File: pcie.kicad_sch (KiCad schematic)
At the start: 21 parts, among them U15 XC7K160T-FFG676

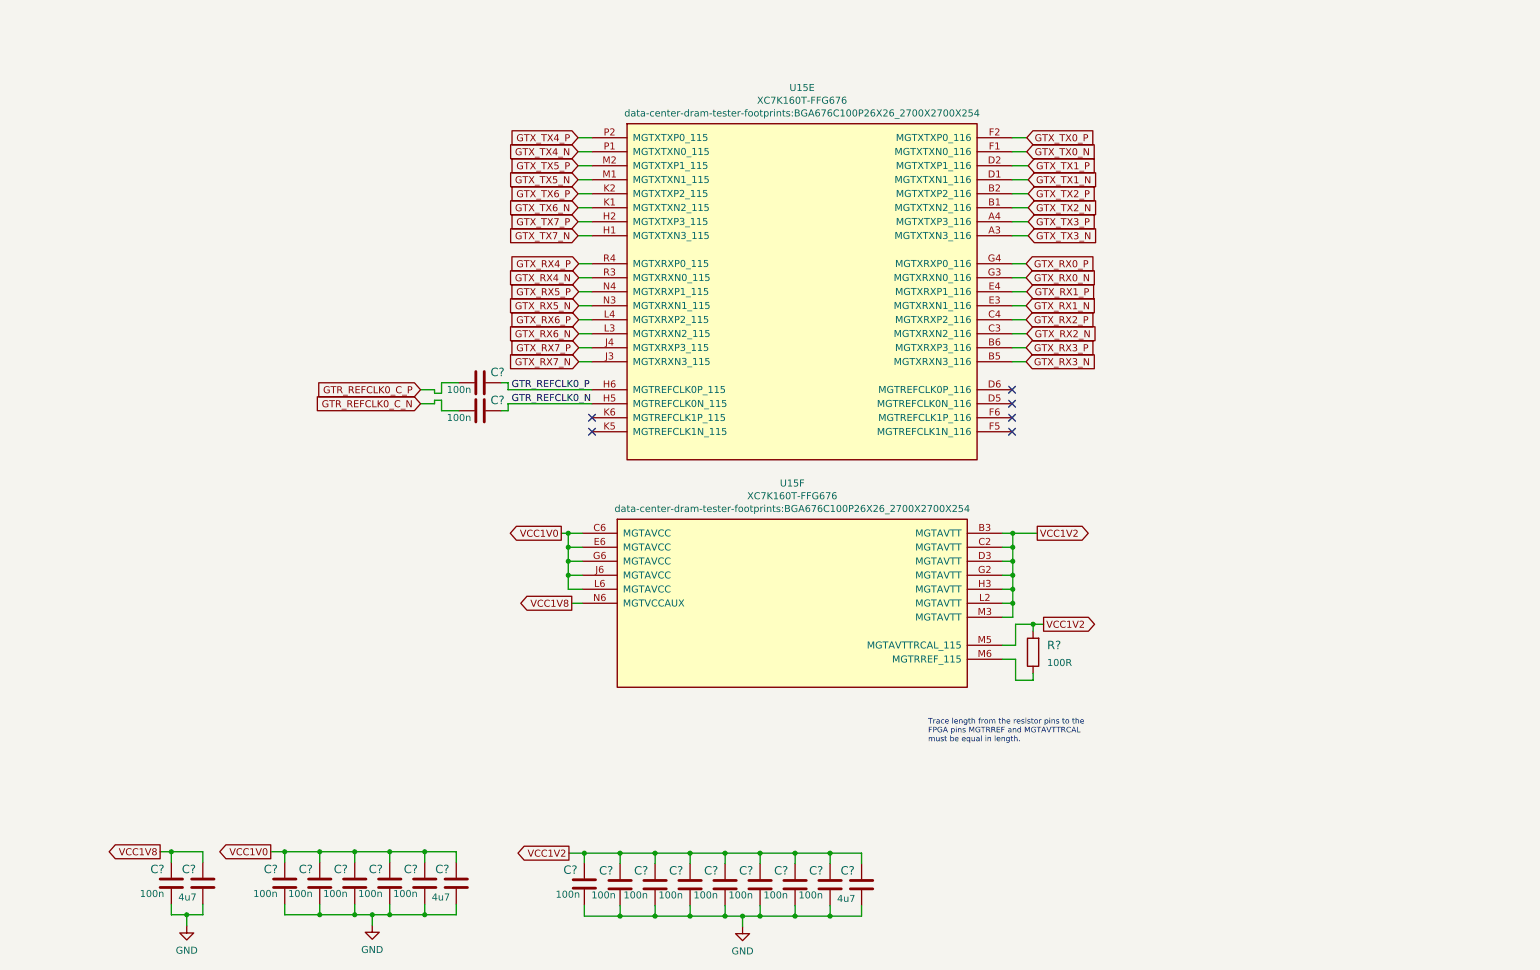
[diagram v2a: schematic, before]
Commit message: Connect ETH mux, connect AUX_JTAG to FMC connector, add RC filter for HOT_SWAP_BUTTON signal
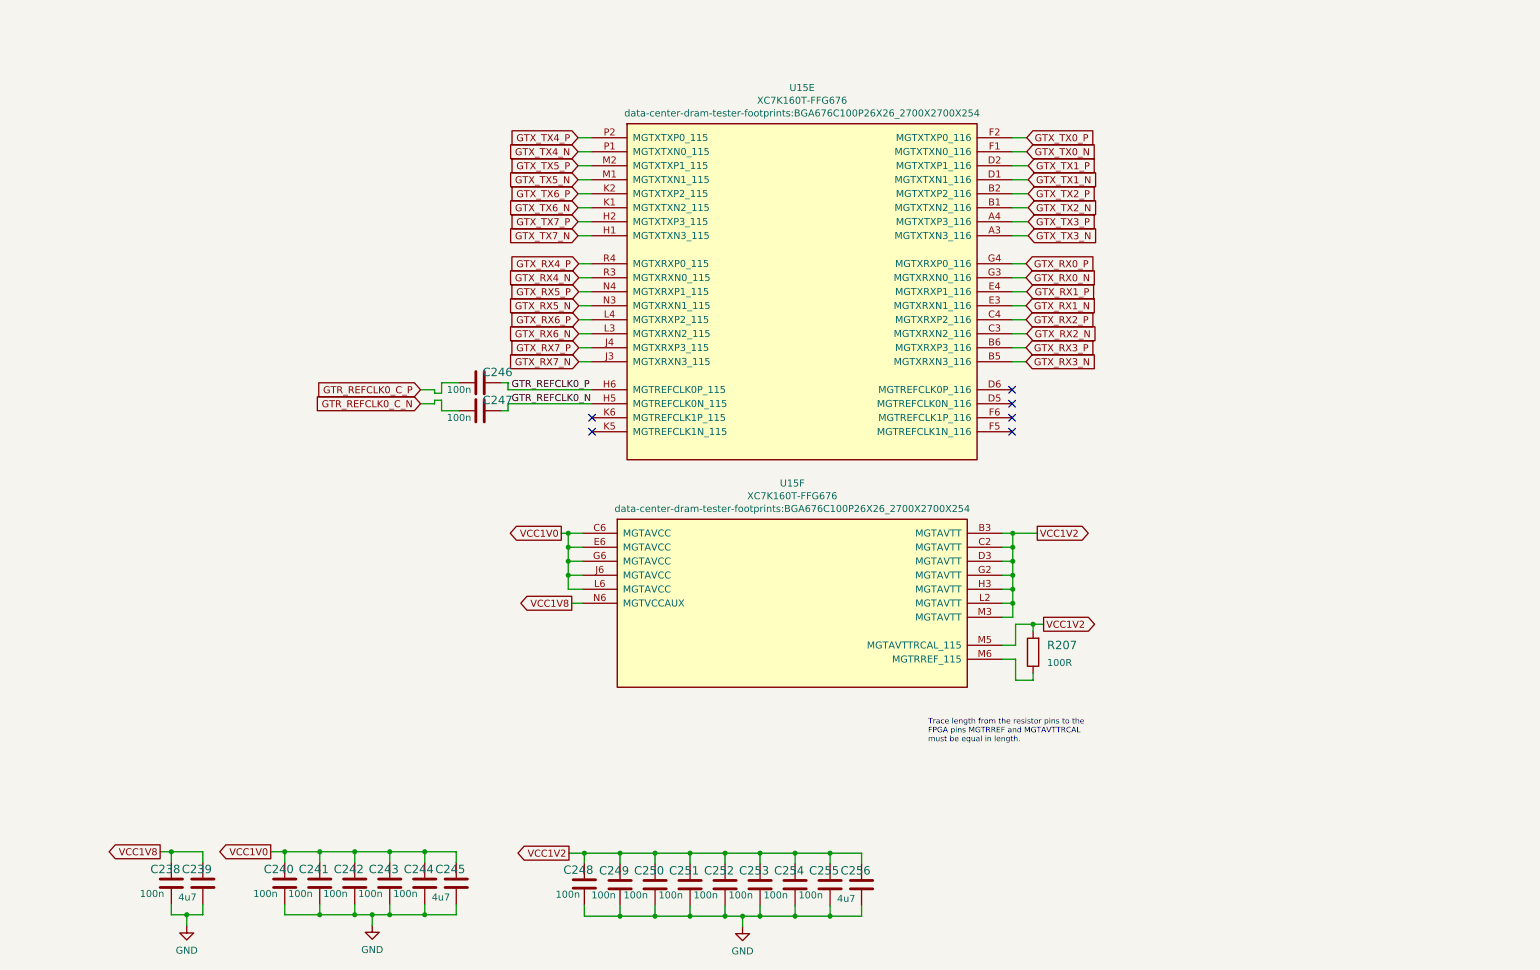
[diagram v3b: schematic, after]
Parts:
- gave numbers to parts that had none: 20
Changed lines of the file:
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@@
   (symbol (lib_id "antmicroCapacitors0402:C_4u7_0402") (at 48.133 178.435 0) (unit 1)
     (in_bom yes) (on_board yes)
-    (property "Reference" "C?" (id 0) (at 44.323 175.895 0)
+    (property "Reference" "C239" (id 0) (at 44.323 175.895 0)
       (effects (font (size 1.524 1.524)) (justify left))
     )
@@
   (symbol (lib_id "antmicroCapacitorsmisc:C_100n_0201") (at 82.042 178.435 0) (unit 1)
     (in_bom yes) (on_board yes)
-    (property "Reference" "C?" (id 0) (at 78.232 175.895 0)
+    (property "Reference" "C243" (id 0) (at 78.232 175.895 0)
       (effects (font (size 1.524 1.524)) (justify left))
     )
@@
   (symbol (lib_id "antmicroCapacitors0402:C_100n_0402") (at 98.425 87.63 90) (unit 1)
     (in_bom yes) (on_board yes)
-    (property "Reference" "C?" (id 0) (at 101.6 85.725 90)
+    (property "Reference" "C246" (id 0) (at 101.6 85.725 90)
       (effects (font (size 1.524 1.524)))
     )
@@
   (symbol (lib_id "antmicroCapacitorsmisc:C_100n_0201") (at 117.348 178.562 0) (unit 1)
     (in_bom yes) (on_board yes)
-    (property "Reference" "C?" (id 0) (at 113.538 176.022 0)
+    (property "Reference" "C248" (id 0) (at 113.538 176.022 0)
       (effects (font (size 1.524 1.524)) (justify left))
     )
@@
   (symbol (lib_id "power:GND") (at 78.867 186.055 0) (unit 1)
     (in_bom yes) (on_board yes) (fields_autoplaced)
-    (property "Reference" "#PWR?" (id 0) (at 78.867 192.405 0)
+    (property "Reference" "#PWR0342" (id 0) (at 78.867 192.405 0)
       (effects (font (size 1.27 1.27)) hide)
     )
@@
   (symbol (lib_id "power:GND") (at 45.212 186.182 0) (unit 1)
     (in_bom yes) (on_board yes) (fields_autoplaced)
-    (property "Reference" "#PWR?" (id 0) (at 45.212 192.532 0)
+    (property "Reference" "#PWR0343" (id 0) (at 45.212 192.532 0)
       (effects (font (size 1.27 1.27)) hide)
     )
@@
   (symbol (lib_id "antmicroCapacitorsmisc:C_100n_0201") (at 149.225 178.689 0) (unit 1)
     (in_bom yes) (on_board yes)
-    (property "Reference" "C?" (id 0) (at 145.415 176.149 0)
+    (property "Reference" "C253" (id 0) (at 145.415 176.149 0)
       (effects (font (size 1.524 1.524)) (justify left))
     )
@@
   (symbol (lib_id "antmicroCapacitorsmisc:C_100n_0201") (at 62.992 178.435 0) (unit 1)
     (in_bom yes) (on_board yes)
-    (property "Reference" "C?" (id 0) (at 59.182 175.895 0)
+    (property "Reference" "C240" (id 0) (at 59.182 175.895 0)
       (effects (font (size 1.524 1.524)) (justify left))
     )
@@
   (symbol (lib_id "antmicroCapacitorsmisc:C_100n_0201") (at 42.418 178.435 0) (unit 1)
     (in_bom yes) (on_board yes)
-    (property "Reference" "C?" (id 0) (at 38.608 175.895 0)
+    (property "Reference" "C238" (id 0) (at 38.608 175.895 0)
       (effects (font (size 1.524 1.524)) (justify left))
     )
@@
   (symbol (lib_id "antmicroCapacitorsmisc:C_100n_0201") (at 130.175 178.689 0) (unit 1)
     (in_bom yes) (on_board yes)
-    (property "Reference" "C?" (id 0) (at 126.365 176.149 0)
+    (property "Reference" "C250" (id 0) (at 126.365 176.149 0)
       (effects (font (size 1.524 1.524)) (justify left))
     )
@@
   (symbol (lib_id "antmicroCapacitorsmisc:C_100n_0201") (at 123.825 178.689 0) (unit 1)
     (in_bom yes) (on_board yes)
-    (property "Reference" "C?" (id 0) (at 120.015 176.149 0)
+    (property "Reference" "C249" (id 0) (at 120.015 176.149 0)
       (effects (font (size 1.524 1.524)) (justify left))
     )
@@
   (symbol (lib_id "antmicroCapacitorsmisc:C_100n_0201") (at 136.525 178.689 0) (unit 1)
     (in_bom yes) (on_board yes)
-    (property "Reference" "C?" (id 0) (at 132.715 176.149 0)
+    (property "Reference" "C251" (id 0) (at 132.715 176.149 0)
       (effects (font (size 1.524 1.524)) (justify left))
     )
@@
   (symbol (lib_id "antmicroCapacitors0402:C_4u7_0402") (at 167.64 178.689 0) (unit 1)
     (in_bom yes) (on_board yes)
-    (property "Reference" "C?" (id 0) (at 163.83 176.149 0)
+    (property "Reference" "C256" (id 0) (at 163.83 176.149 0)
       (effects (font (size 1.524 1.524)) (justify left))
     )
@@
   (symbol (lib_id "antmicroCapacitorsmisc:C_100n_0201") (at 75.692 178.435 0) (unit 1)
     (in_bom yes) (on_board yes)
-    (property "Reference" "C?" (id 0) (at 71.882 175.895 0)
+    (property "Reference" "C242" (id 0) (at 71.882 175.895 0)
       (effects (font (size 1.524 1.524)) (justify left))
     )
@@
   (symbol (lib_id "antmicroCapacitorsmisc:C_100n_0201") (at 69.342 178.435 0) (unit 1)
     (in_bom yes) (on_board yes)
-    (property "Reference" "C?" (id 0) (at 65.532 175.895 0)
+    (property "Reference" "C241" (id 0) (at 65.532 175.895 0)
       (effects (font (size 1.524 1.524)) (justify left))
     )
@@
   (symbol (lib_id "antmicroCapacitorsmisc:C_100n_0201") (at 155.575 178.689 0) (unit 1)
     (in_bom yes) (on_board yes)
-    (property "Reference" "C?" (id 0) (at 151.765 176.149 0)
+    (property "Reference" "C254" (id 0) (at 151.765 176.149 0)
       (effects (font (size 1.524 1.524)) (justify left))
     )
@@
   (symbol (lib_id "antmicroResistors0402:R_100R_0402") (at 198.755 136.525 90) (unit 1)
     (in_bom yes) (on_board yes) (fields_autoplaced)
-    (property "Reference" "R?" (id 0) (at 201.295 135.255 90)
+    (property "Reference" "R207" (id 0) (at 201.295 135.255 90)
       (effects (font (size 1.524 1.524)) (justify right))
     )
@@
   (symbol (lib_id "power:GND") (at 146.05 186.309 0) (unit 1)
     (in_bom yes) (on_board yes) (fields_autoplaced)
-    (property "Reference" "#PWR?" (id 0) (at 146.05 192.659 0)
+    (property "Reference" "#PWR0341" (id 0) (at 146.05 192.659 0)
       (effects (font (size 1.27 1.27)) hide)
     )
@@
   (symbol (lib_id "antmicroCapacitors0402:C_4u7_0402") (at 94.107 178.435 0) (unit 1)
     (in_bom yes) (on_board yes)
-    (property "Reference" "C?" (id 0) (at 90.297 175.895 0)
+    (property "Reference" "C245" (id 0) (at 90.297 175.895 0)
       (effects (font (size 1.524 1.524)) (justify left))
     )
@@
   (symbol (lib_id "antmicroCapacitorsmisc:C_100n_0201") (at 88.392 178.435 0) (unit 1)
     (in_bom yes) (on_board yes)
-    (property "Reference" "C?" (id 0) (at 84.582 175.895 0)
+    (property "Reference" "C244" (id 0) (at 84.582 175.895 0)
       (effects (font (size 1.524 1.524)) (justify left))
     )
@@
   (symbol (lib_id "antmicroCapacitors0402:C_100n_0402") (at 98.425 92.71 90) (unit 1)
     (in_bom yes) (on_board yes)
-    (property "Reference" "C?" (id 0) (at 101.6 90.805 90)
+    (property "Reference" "C247" (id 0) (at 101.6 90.805 90)
       (effects (font (size 1.524 1.524)))
     )
@@
   (symbol (lib_id "antmicroCapacitorsmisc:C_100n_0201") (at 142.875 178.689 0) (unit 1)
     (in_bom yes) (on_board yes)
-    (property "Reference" "C?" (id 0) (at 139.065 176.149 0)
+    (property "Reference" "C252" (id 0) (at 139.065 176.149 0)
       (effects (font (size 1.524 1.524)) (justify left))
     )
@@
   (symbol (lib_id "antmicroCapacitorsmisc:C_100n_0201") (at 161.925 178.689 0) (unit 1)
     (in_bom yes) (on_board yes)
-    (property "Reference" "C?" (id 0) (at 158.115 176.149 0)
+    (property "Reference" "C255" (id 0) (at 158.115 176.149 0)
       (effects (font (size 1.524 1.524)) (justify left))
     )

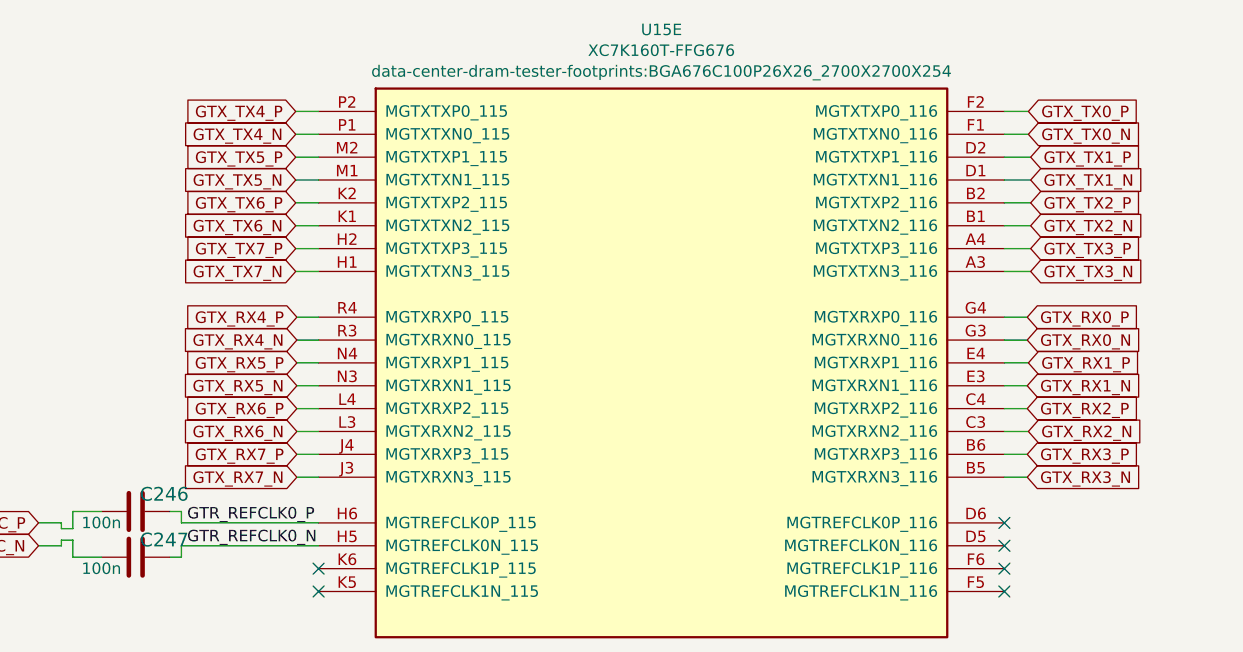
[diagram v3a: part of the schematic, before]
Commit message: Correct PCIe pin assigment, replace MODE2 symbol, export changes to PCB, progess in the new components placement
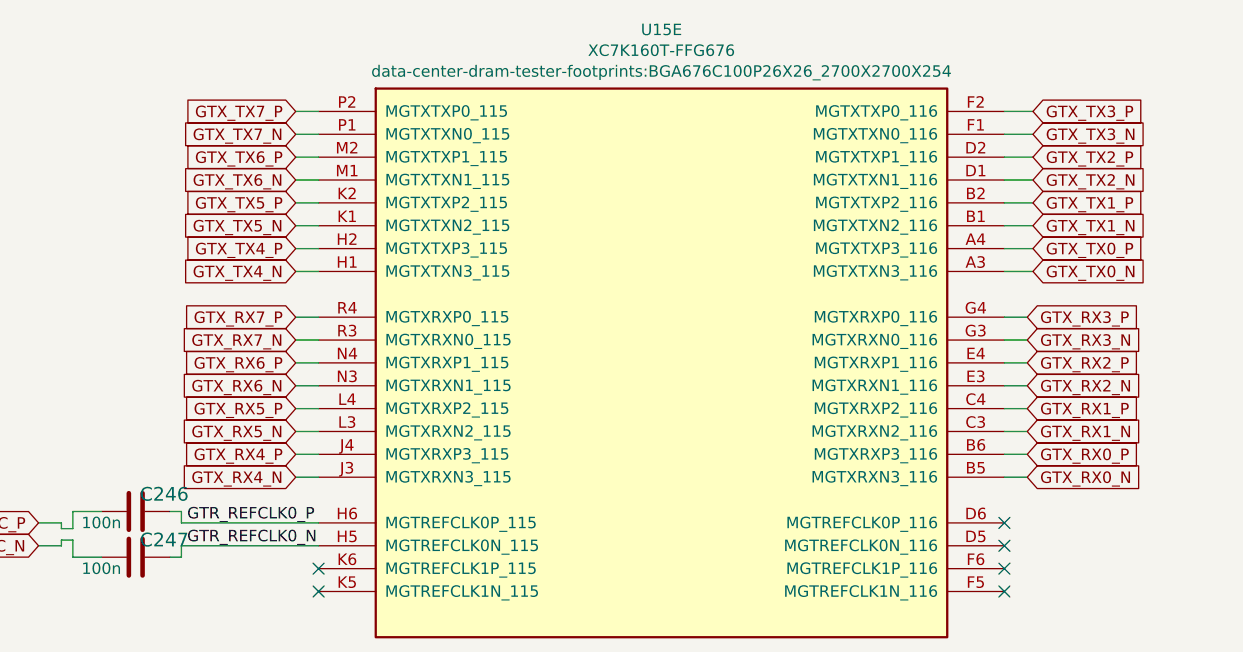
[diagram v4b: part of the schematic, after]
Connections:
- net GTX_RX0_N: now also U15.B5 (MGTXRXN3_116); no longer U15.G3 (MGTXRXN0_116)
- net GTX_RX0_P: now also U15.B6 (MGTXRXP3_116); no longer U15.G4 (MGTXRXP0_116)
- net GTX_RX1_N: now also U15.C3 (MGTXRXN2_116); no longer U15.E3 (MGTXRXN1_116)
- net GTX_RX1_P: now also U15.C4 (MGTXRXP2_116); no longer U15.E4 (MGTXRXP1_116)
- net GTX_RX2_N: now also U15.E3 (MGTXRXN1_116); no longer U15.C3 (MGTXRXN2_116)
- net GTX_RX2_P: now also U15.E4 (MGTXRXP1_116); no longer U15.C4 (MGTXRXP2_116)
- net GTX_RX3_N: now also U15.G3 (MGTXRXN0_116); no longer U15.B5 (MGTXRXN3_116)
- net GTX_RX3_P: now also U15.G4 (MGTXRXP0_116); no longer U15.B6 (MGTXRXP3_116)
- net GTX_RX4_N: now also U15.J3 (MGTXRXN3_115); no longer U15.R3 (MGTXRXN0_115)
- net GTX_RX4_P: now also U15.J4 (MGTXRXP3_115); no longer U15.R4 (MGTXRXP0_115)
- net GTX_RX5_N: now also U15.L3 (MGTXRXN2_115); no longer U15.N3 (MGTXRXN1_115)
- net GTX_RX5_P: now also U15.L4 (MGTXRXP2_115); no longer U15.N4 (MGTXRXP1_115)
- net GTX_RX6_N: now also U15.N3 (MGTXRXN1_115); no longer U15.L3 (MGTXRXN2_115)
- net GTX_RX6_P: now also U15.N4 (MGTXRXP1_115); no longer U15.L4 (MGTXRXP2_115)
- net GTX_RX7_N: now also U15.R3 (MGTXRXN0_115); no longer U15.J3 (MGTXRXN3_115)
- net GTX_RX7_P: now also U15.R4 (MGTXRXP0_115); no longer U15.J4 (MGTXRXP3_115)
- net GTX_TX0_N: now also U15.A3 (MGTXTXN3_116); no longer U15.F1 (MGTXTXN0_116)
- net GTX_TX0_P: now also U15.A4 (MGTXTXP3_116); no longer U15.F2 (MGTXTXP0_116)
- net GTX_TX1_N: now also U15.B1 (MGTXTXN2_116); no longer U15.D1 (MGTXTXN1_116)
- net GTX_TX1_P: now also U15.B2 (MGTXTXP2_116); no longer U15.D2 (MGTXTXP1_116)
- net GTX_TX2_N: now also U15.D1 (MGTXTXN1_116); no longer U15.B1 (MGTXTXN2_116)
- net GTX_TX2_P: now also U15.D2 (MGTXTXP1_116); no longer U15.B2 (MGTXTXP2_116)
- net GTX_TX3_N: now also U15.F1 (MGTXTXN0_116); no longer U15.A3 (MGTXTXN3_116)
- net GTX_TX3_P: now also U15.F2 (MGTXTXP0_116); no longer U15.A4 (MGTXTXP3_116)
- net GTX_TX4_N: now also U15.H1 (MGTXTXN3_115); no longer U15.P1 (MGTXTXN0_115)
- net GTX_TX4_P: now also U15.H2 (MGTXTXP3_115); no longer U15.P2 (MGTXTXP0_115)
- net GTX_TX5_N: now also U15.K1 (MGTXTXN2_115); no longer U15.M1 (MGTXTXN1_115)
- net GTX_TX5_P: now also U15.K2 (MGTXTXP2_115); no longer U15.M2 (MGTXTXP1_115)
- net GTX_TX6_N: now also U15.M1 (MGTXTXN1_115); no longer U15.K1 (MGTXTXN2_115)
- net GTX_TX6_P: now also U15.M2 (MGTXTXP1_115); no longer U15.K2 (MGTXTXP2_115)
- net GTX_TX7_N: now also U15.P1 (MGTXTXN0_115); no longer U15.H1 (MGTXTXN3_115)
- net GTX_TX7_P: now also U15.P2 (MGTXTXP0_115); no longer U15.H2 (MGTXTXP3_115)
